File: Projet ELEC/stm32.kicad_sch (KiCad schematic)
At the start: 13 parts, among them SW1 SW_Push, U8 STM32F103RBTx

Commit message: corrected around 60 errors, removed a 74ls04, and many other improvements
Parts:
- BZ1: footprint (none) -> Buzzer_Beeper:Buzzer_TDK_PS1240P02BT_D12.2mm_H6.5mm
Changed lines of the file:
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@@
+				)
+			)
+			(project "Projet ELEC"
+				(path "/2d0c4a09-24e5-4892-bf2e-0a851a14e0ff/9bbe7e6a-d830-471e-900b-a555ab0eb406"
+					(reference "C7")
+					(unit 1)
 				)
 			)
@@
 				)
 			)
+			(project "Projet ELEC"
+				(path "/2d0c4a09-24e5-4892-bf2e-0a851a14e0ff/9bbe7e6a-d830-471e-900b-a555ab0eb406"
+					(reference "C3")
+					(unit 1)
+				)
+			)
 		)
 	)
@@
 				)
 			)
+			(project "Projet ELEC"
+				(path "/2d0c4a09-24e5-4892-bf2e-0a851a14e0ff/9bbe7e6a-d830-471e-900b-a555ab0eb406"
+					(reference "C10")
+					(unit 1)
+				)
+			)
 		)
 	)
@@
 				)
 			)
+			(project "Projet ELEC"
+				(path "/2d0c4a09-24e5-4892-bf2e-0a851a14e0ff/9bbe7e6a-d830-471e-900b-a555ab0eb406"
+					(reference "#PWR013")
+					(unit 1)
+				)
+			)
 		)
 	)
@@
 				)
 			)
+			(project "Projet ELEC"
+				(path "/2d0c4a09-24e5-4892-bf2e-0a851a14e0ff/9bbe7e6a-d830-471e-900b-a555ab0eb406"
+					(reference "C8")
+					(unit 1)
+				)
+			)
 		)
 	)
@@
 				)
 			)
+			(project "Projet ELEC"
+				(path "/2d0c4a09-24e5-4892-bf2e-0a851a14e0ff/9bbe7e6a-d830-471e-900b-a555ab0eb406"
+					(reference "C1")
+					(unit 1)
+				)
+			)
 		)
 	)
@@
 				)
 			)
+			(project "Projet ELEC"
+				(path "/2d0c4a09-24e5-4892-bf2e-0a851a14e0ff/9bbe7e6a-d830-471e-900b-a555ab0eb406"
+					(reference "C9")
+					(unit 1)
+				)
+			)
 		)
 	)
@@
 				)
 			)
+			(project "Projet ELEC"
+				(path "/2d0c4a09-24e5-4892-bf2e-0a851a14e0ff/9bbe7e6a-d830-471e-900b-a555ab0eb406"
+					(reference "U8")
+					(unit 1)
+				)
+			)
 		)
 	)
@@
 				)
 			)
+			(project "Projet ELEC"
+				(path "/2d0c4a09-24e5-4892-bf2e-0a851a14e0ff/9bbe7e6a-d830-471e-900b-a555ab0eb406"
+					(reference "#PWR010")
+					(unit 1)
+				)
+			)
 		)
 	)
@@
 				)
 			)
+			(project "Projet ELEC"
+				(path "/2d0c4a09-24e5-4892-bf2e-0a851a14e0ff/9bbe7e6a-d830-471e-900b-a555ab0eb406"
+					(reference "C5")
+					(unit 1)
+				)
+			)
 		)
 	)
@@
 				)
 			)
+			(project "Projet ELEC"
+				(path "/2d0c4a09-24e5-4892-bf2e-0a851a14e0ff/9bbe7e6a-d830-471e-900b-a555ab0eb406"
+					(reference "C2")
+					(unit 1)
+				)
+			)
 		)
 	)
@@
 				)
 			)
+			(project "Projet ELEC"
+				(path "/2d0c4a09-24e5-4892-bf2e-0a851a14e0ff/9bbe7e6a-d830-471e-900b-a555ab0eb406"
+					(reference "#PWR012")
+					(unit 1)
+				)
+			)
 		)
 	)
@@
 				)
 			)
+			(project "Projet ELEC"
+				(path "/2d0c4a09-24e5-4892-bf2e-0a851a14e0ff/9bbe7e6a-d830-471e-900b-a555ab0eb406"
+					(reference "#PWR09")
+					(unit 1)
+				)
+			)
 		)
 	)
@@
 				)
 			)
+			(project "Projet ELEC"
+				(path "/2d0c4a09-24e5-4892-bf2e-0a851a14e0ff/9bbe7e6a-d830-471e-900b-a555ab0eb406"
+					(reference "C4")
+					(unit 1)
+				)
+			)
 		)
 	)
@@
 				)
 			)
+			(project "Projet ELEC"
+				(path "/2d0c4a09-24e5-4892-bf2e-0a851a14e0ff/9bbe7e6a-d830-471e-900b-a555ab0eb406"
+					(reference "C6")
+					(unit 1)
+				)
+			)
 		)
 	)
@@
 				)
 			)
+			(project "Projet ELEC"
+				(path "/2d0c4a09-24e5-4892-bf2e-0a851a14e0ff/9bbe7e6a-d830-471e-900b-a555ab0eb406"
+					(reference "reset_btn1")
+					(unit 1)
+				)
+			)
 		)
 	)
@@
 				)
 			)
+			(project "Projet ELEC"
+				(path "/2d0c4a09-24e5-4892-bf2e-0a851a14e0ff/9bbe7e6a-d830-471e-900b-a555ab0eb406"
+					(reference "#PWR011")
+					(unit 1)
+				)
+			)
 		)
 	)
@@
 			)
 		)
-		(property "Footprint" ""
+		(property "Footprint" "Buzzer_Beeper:Buzzer_TDK_PS1240P02BT_D12.2mm_H6.5mm"
 			(at 142.875 76.2 90)
 			(effects
@@
 					(reference "BZ1")
 					(unit 1)
+				)
+			)
+			(project "Projet ELEC"
+				(path "/2d0c4a09-24e5-4892-bf2e-0a851a14e0ff/9bbe7e6a-d830-471e-900b-a555ab0eb406"
+					(reference "BZ1")
+					(unit 1)

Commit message: on va mourir mdr
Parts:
- SW1: footprint Button_Switch_SMD:SW_Push_1P1T_NO_CK_PTS125Sx43PSMTR -> Button_Switch_THT:SW_PUSH_6mm
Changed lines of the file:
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@@
 			)
 		)
-		(property "Footprint" "Button_Switch_SMD:SW_Push_1P1T_NO_CK_PTS125Sx43PSMTR"
+		(property "Footprint" "Button_Switch_THT:SW_PUSH_6mm"
 			(at 72.39 53.34 0)
 			(effects

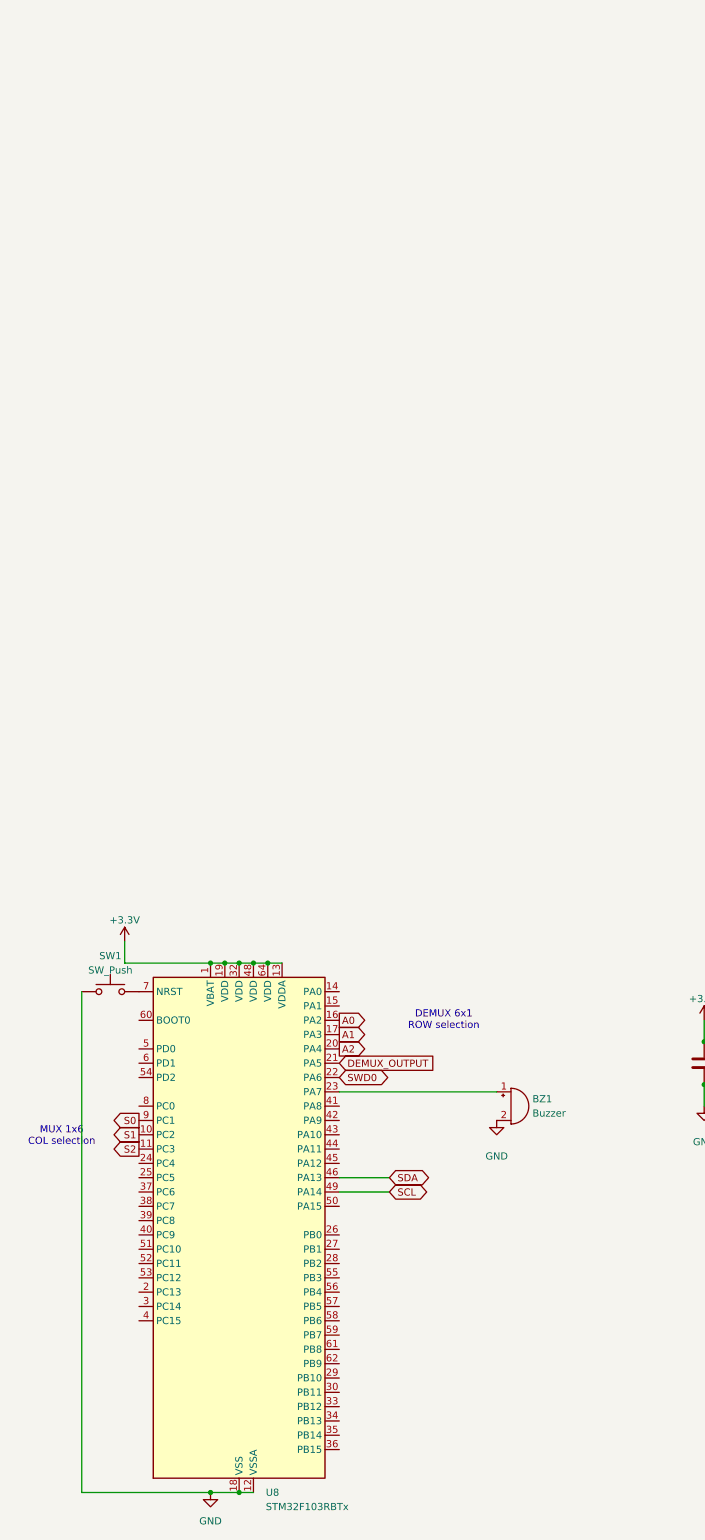
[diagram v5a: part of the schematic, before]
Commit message: feat(stm32): schematics for f103
* Projet ELEC/stm32.kicad_sch
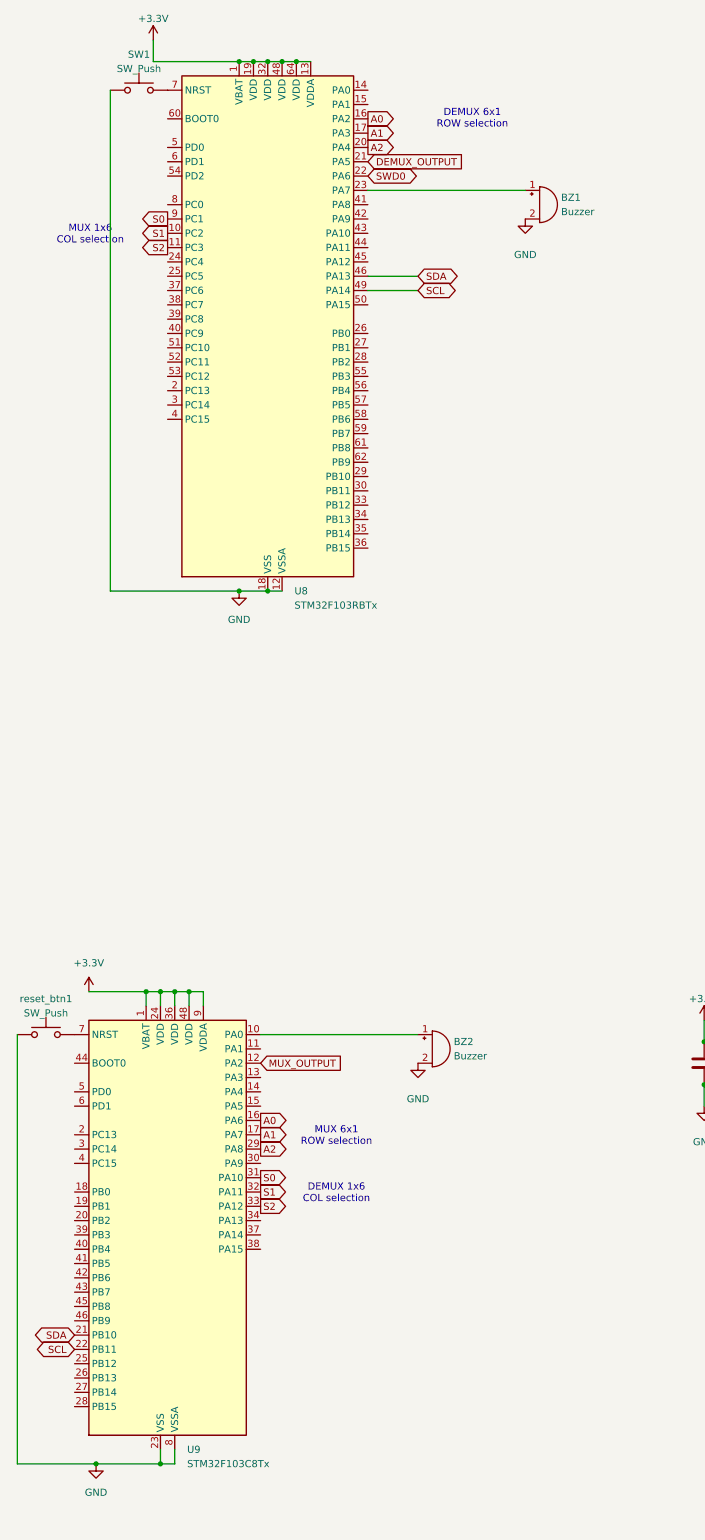
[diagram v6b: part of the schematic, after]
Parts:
- added BZ2: Buzzer, Buzzer_Beeper:Buzzer_TDK_PS1240P02BT_D12.2mm_H6.5mm, symbol Device:Buzzer
- added U9: STM32F103C8Tx, Package_QFP:LQFP-48_7x7mm_P0.5mm, symbol MCU_ST_STM32F1:STM32F103C8Tx
- added reset_btn1: SW_Push, Button_Switch_SMD:SW_Push_1P1T_NO_CK_PTS125Sx43PSMTR, symbol Switch:SW_Push
- SW1: footprint Button_Switch_THT:SW_PUSH_6mm -> Button_Switch_SMD:SW_Push_1P1T_NO_CK_PTS125Sx43PSMTR
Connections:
- net +3.3V: now also U9.1 (VBAT), U9.24 (VDD), U9.36 (VDD), U9.48 (VDD), U9.9 (VDDA)
- net A0: now also U9.16 (PA6)
- net A1: now also U9.17 (PA7)
- net A2: now also U9.29 (PA8)
- net GND: now also BZ2.2 (-), U9.23 (VSS), U9.35 (VSS), U9.47 (VSS), U9.8 (VSSA), reset_btn1.1
- net S0: now also U9.31 (PA10)
- net S1: now also U9.32 (PA11)
- net S2: now also U9.33 (PA12)
- net SCL: now also U9.22 (PB11)
- net SDA: now also U9.21 (PB10)
- new net: U9.7 (NRST), reset_btn1.2
- new net: BZ2.1 (+), U9.10 (PA0)
- new net MUX_OUTPUT: U9.12 (PA2)
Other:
- note added: "DEMUX 1x6 COL selection"
- note added: "MUX 6x1 ROW selection"
- moved on the sheet: BZ1, SW1, U8

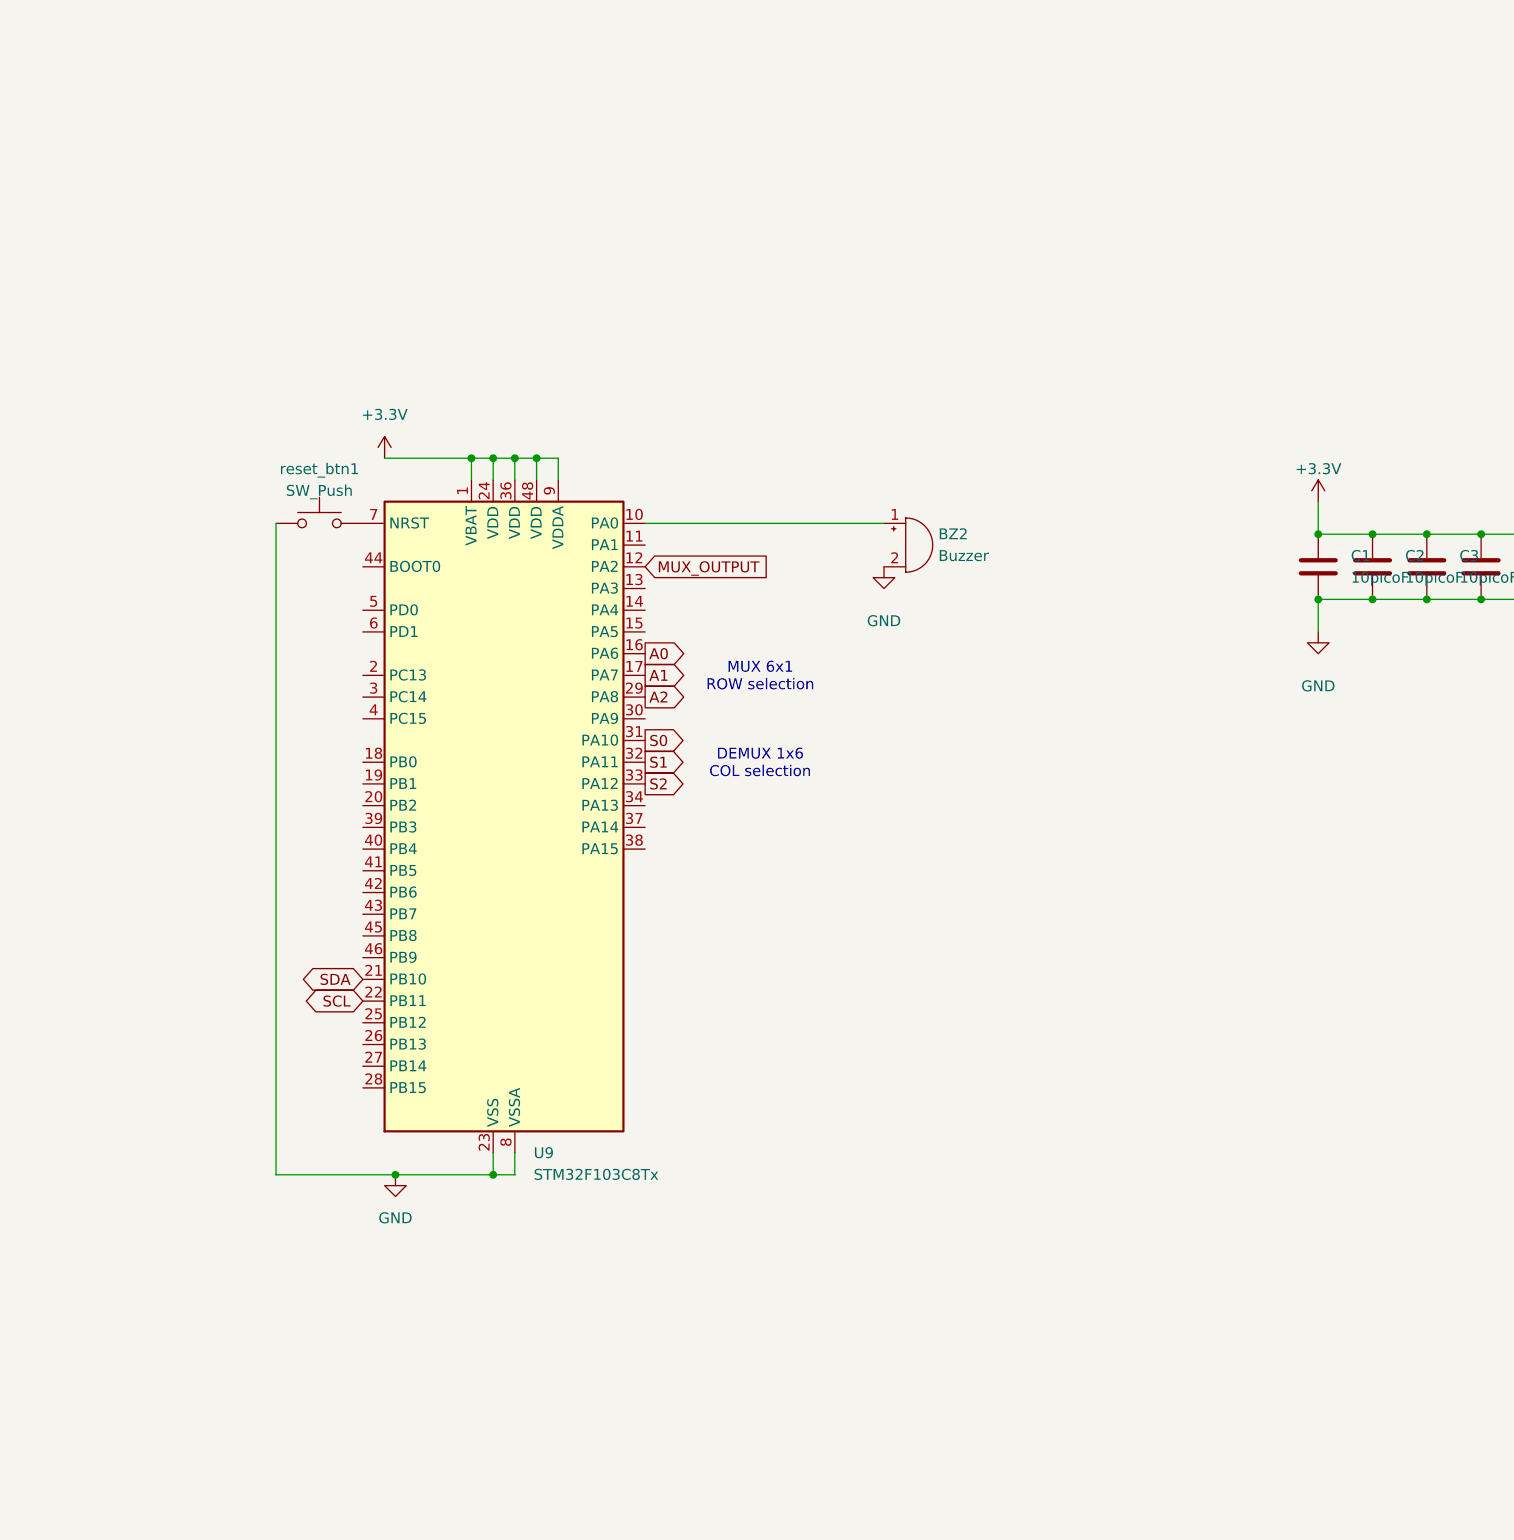
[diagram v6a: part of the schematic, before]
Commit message: feat(st-link): add nucleo 64-l476rg + connect to f103 through swd
* Projet ELEC/stm32.kicad_sch
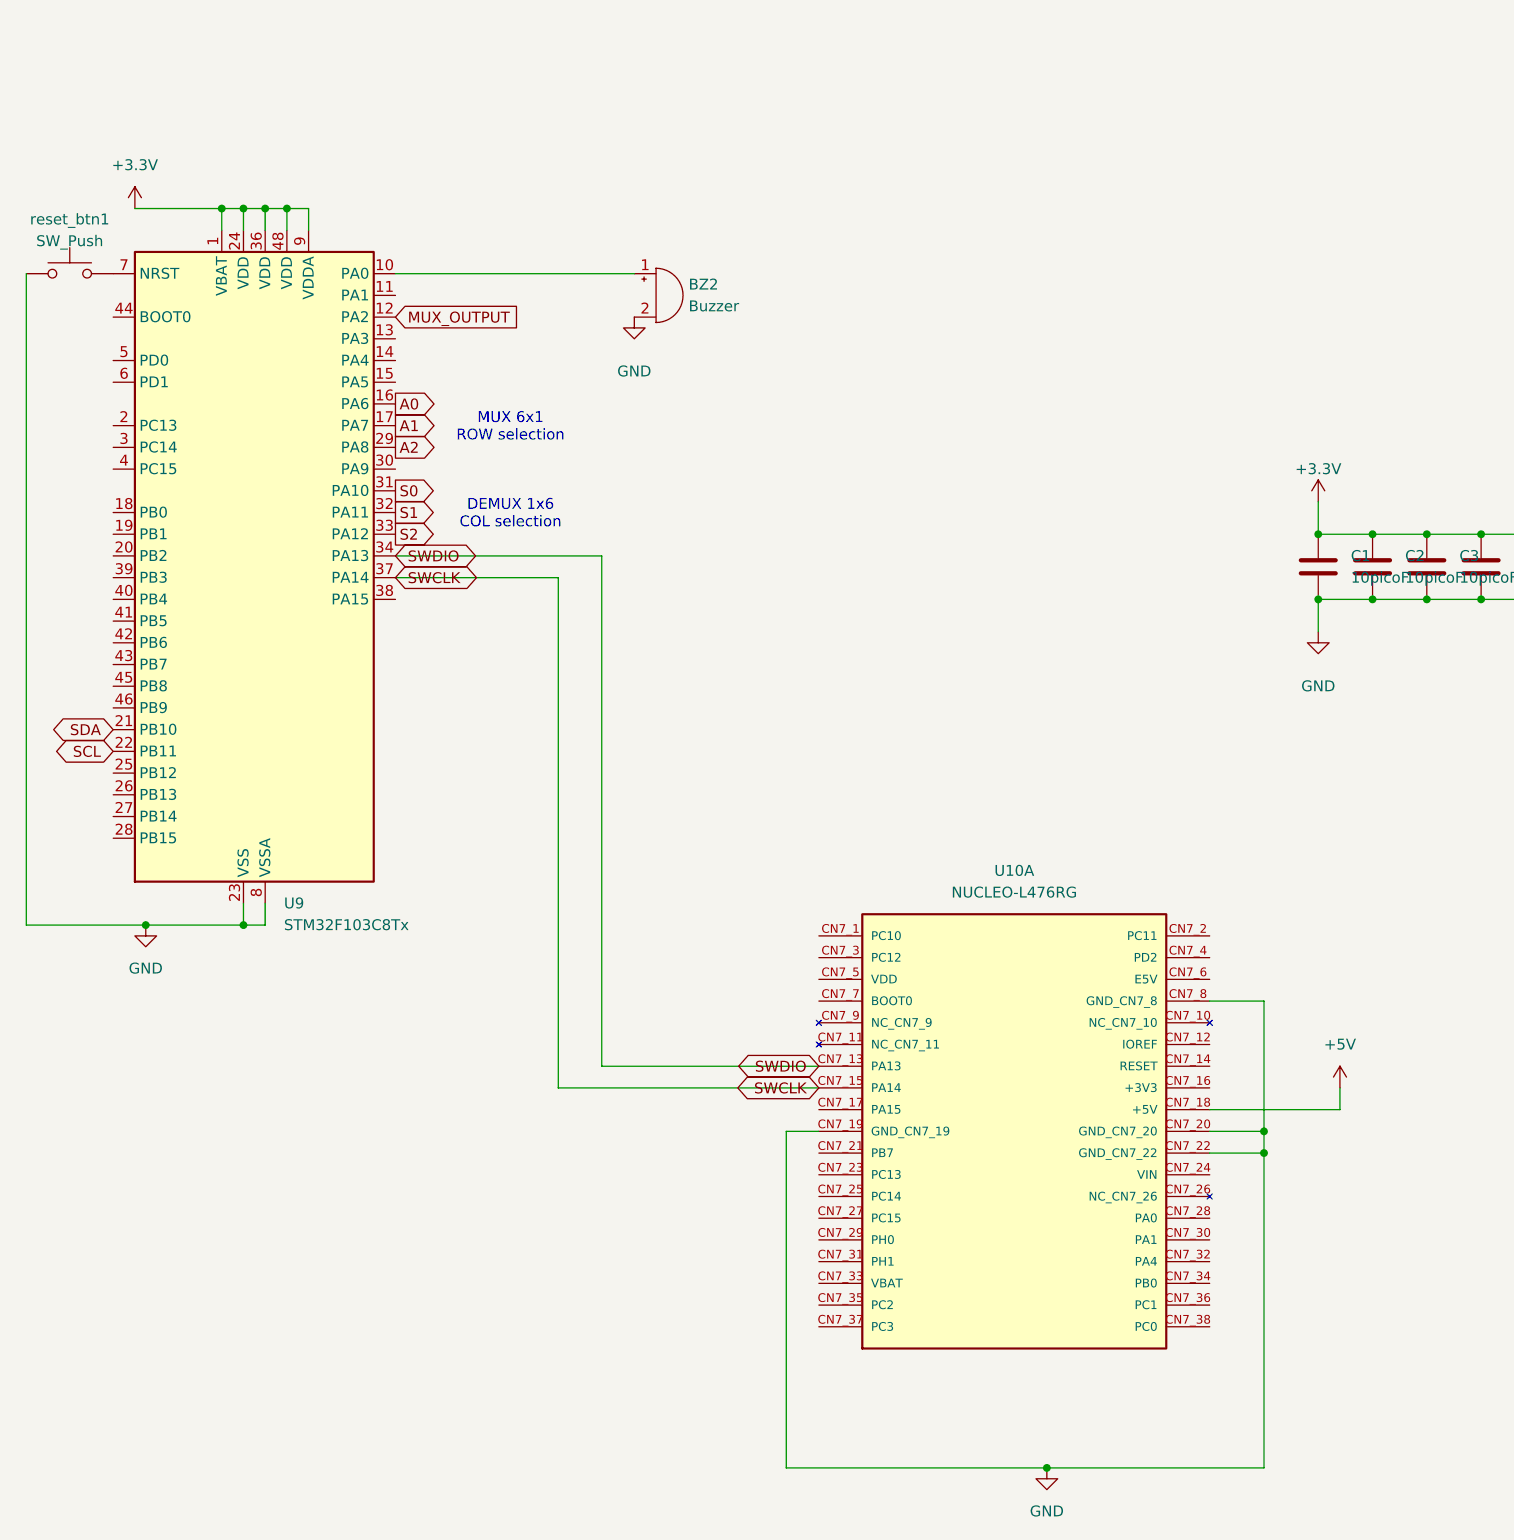
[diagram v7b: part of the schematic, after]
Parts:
- added U10: NUCLEO-L476RG, NUCLEO-L476RG:MODULE_NUCLEO-L476RG, symbol NUCLEO-L476RG:NUCLEO-L476RG
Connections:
- net GND: now also U10.CN7_19 (GND_CN7_19), U10.CN7_20 (GND_CN7_20), U10.CN7_22 (GND_CN7_22), U10.CN7_8 (GND_CN7_8)
- net SWDIO: now reaches U9.34 (PA13)
- net SWDIO: now also U10.CN7_13 (PA13)
- net SWCLK: now reaches U9.37 (PA14)
- net SWCLK: now also U10.CN7_15 (PA14)
- new net +5V: U10.CN7_18 (+5V)
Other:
- moved on the sheet: BZ2, U9, reset_btn1

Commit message: [*] stm32 schematics
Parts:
- removed U10: NUCLEO-L476RG, NUCLEO-L476RG:MODULE_NUCLEO-L476RG, symbol NUCLEO-L476RG:NUCLEO-L476RG
- removed reset_btn1: SW_Push, Button_Switch_SMD:SW_Push_1P1T_NO_CK_PTS125Sx43PSMTR, symbol Switch:SW_Push
- added 3v3, GND, NRST, SWCLK, SWDIO: Conn_01x01_MountingPin, Connector_PinHeader_1.00mm:PinHeader_1x01_P1.00mm_Vertical, symbol Connector_Generic_MountingPin:Conn_01x01_MountingPin
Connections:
- net +3.3V: no longer U9.1 (VBAT), U9.24 (VDD), U9.36 (VDD), U9.48 (VDD), U9.9 (VDDA)
- net GND: no longer U9.23 (VSS), U9.35 (VSS), U9.47 (VSS), U9.8 (VSSA)
- net at U9.7 (NRST): now also NRST.MP (MountPin)
- net SWCLK: no longer names the net of U9.37 (PA14)
- net SWCLK: now also SWCLK.MP (MountPin)
- net SWDIO: no longer names the net of U9.34 (PA13)
- net SWDIO: now also SWDIO.MP (MountPin)
- new net: 3v3.MP (MountPin), U9.1 (VBAT), U9.24 (VDD), U9.36 (VDD), U9.48 (VDD), U9.9 (VDDA)
- new net: GND.MP (MountPin), U9.23 (VSS), U9.35 (VSS), U9.47 (VSS), U9.8 (VSSA)
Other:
- moved on the sheet: BZ2, C1, C10, C2, C3, C4, C5, C6, C7, C8, C9, U9
